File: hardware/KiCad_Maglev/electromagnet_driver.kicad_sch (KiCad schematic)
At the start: 29 parts, among them J5 621008245821, J6 621006245821

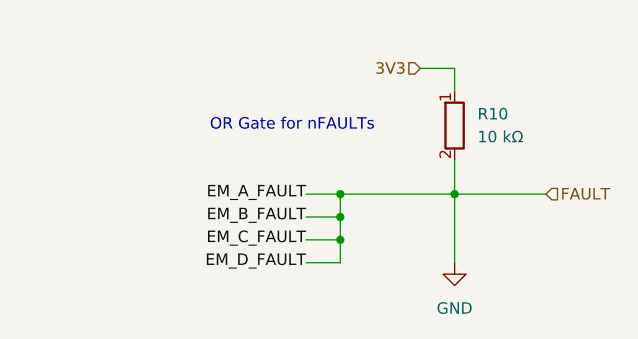
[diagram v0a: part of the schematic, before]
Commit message: some changes to pcb schmatic, added datasheets for used components and linked wurth repo
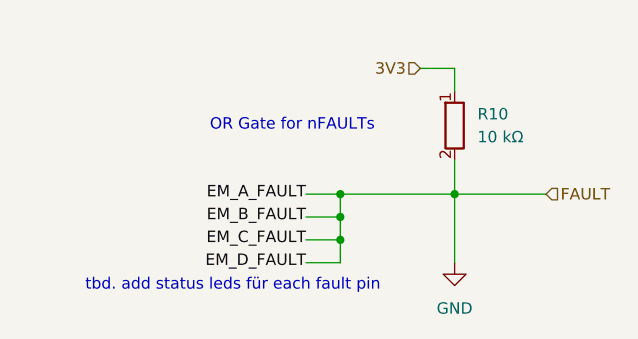
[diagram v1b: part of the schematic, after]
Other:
- note added: "tbd. add status leds für each fault pin"
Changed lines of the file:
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@@
+		)
+	)
+	(text "tbd. add status leds für each fault pin"
+		(exclude_from_sim no)
+		(at 35.052 185.42 0)
+		(effects
+			(font
+				(size 1.27 1.27)
+			)
 		)
 	)

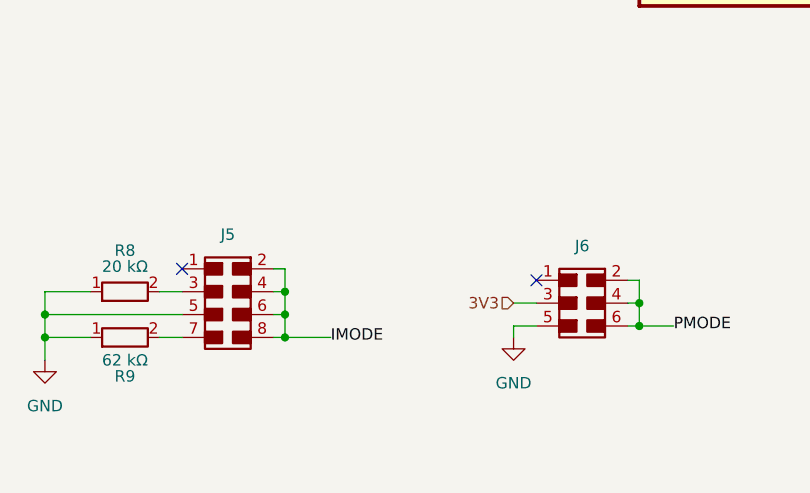
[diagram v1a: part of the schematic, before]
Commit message: Update KiCad schematic sheets
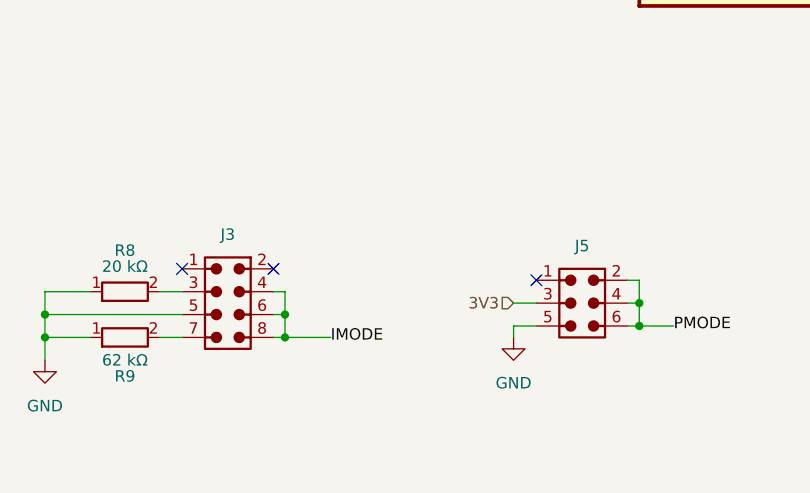
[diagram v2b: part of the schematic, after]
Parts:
- removed J5: 621008245821, Connector_SMD_Wurth:J_Wurth_WR-PHD_621008245821, symbol Connector_Wurth_WR-PHD:621008245821
- removed J6: 621006245821, Connector_SMD_Wurth:J_Wurth_WR-PHD_621006245821, symbol Connector_Wurth_WR-PHD:621006245821
- added J3: 61300821121, Connector_THT_Wurth:J_Wurth_WR-PHD_61300821121, symbol Connector_Wurth_WR-PHD:61300821121
- added J5: 61300621121, Connector_THT_Wurth:J_Wurth_WR-PHD_61300621121, symbol Connector_Wurth_WR-PHD:61300621121
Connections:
- net 3V3: now also J5.3
- net GND: now also J3.5, J5.5
- net IMODE: now also J3.4, J3.6, J3.8
- net PMODE: now also J5.2, J5.4, J5.6
- net at R8.2: now also J3.3
- net at R9.2: now also J3.7
- no-connect marks 2 -> 3

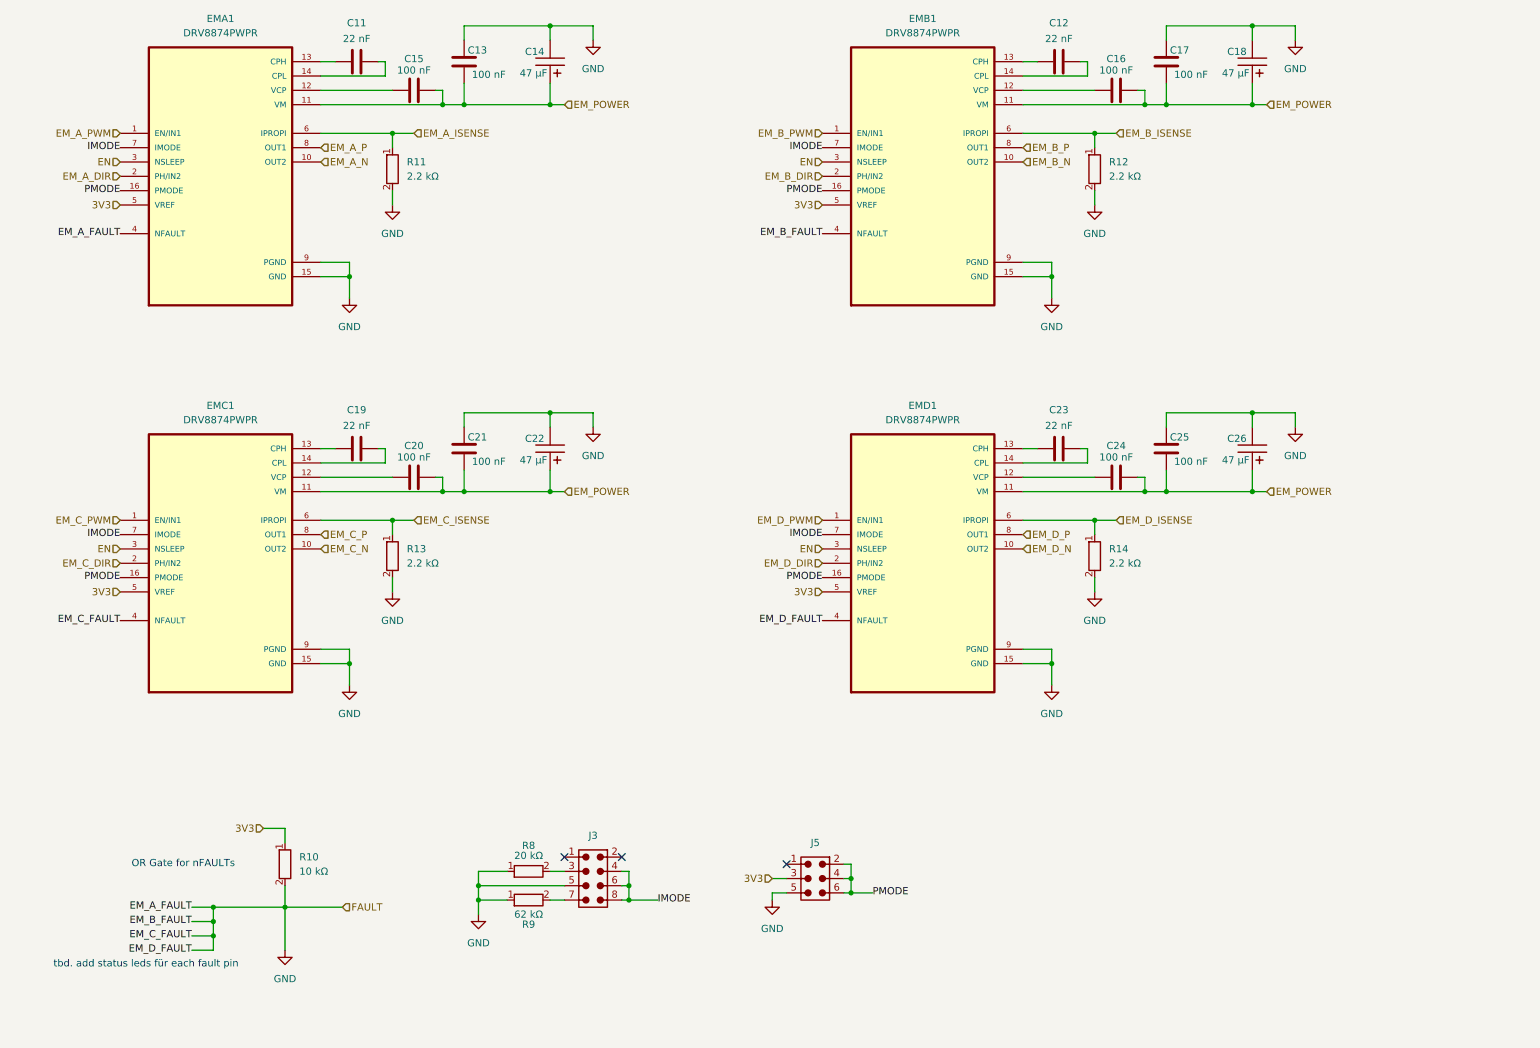
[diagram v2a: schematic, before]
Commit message: Added Footprints/Models for coil and ringmagnet, changed most components to 1206 series
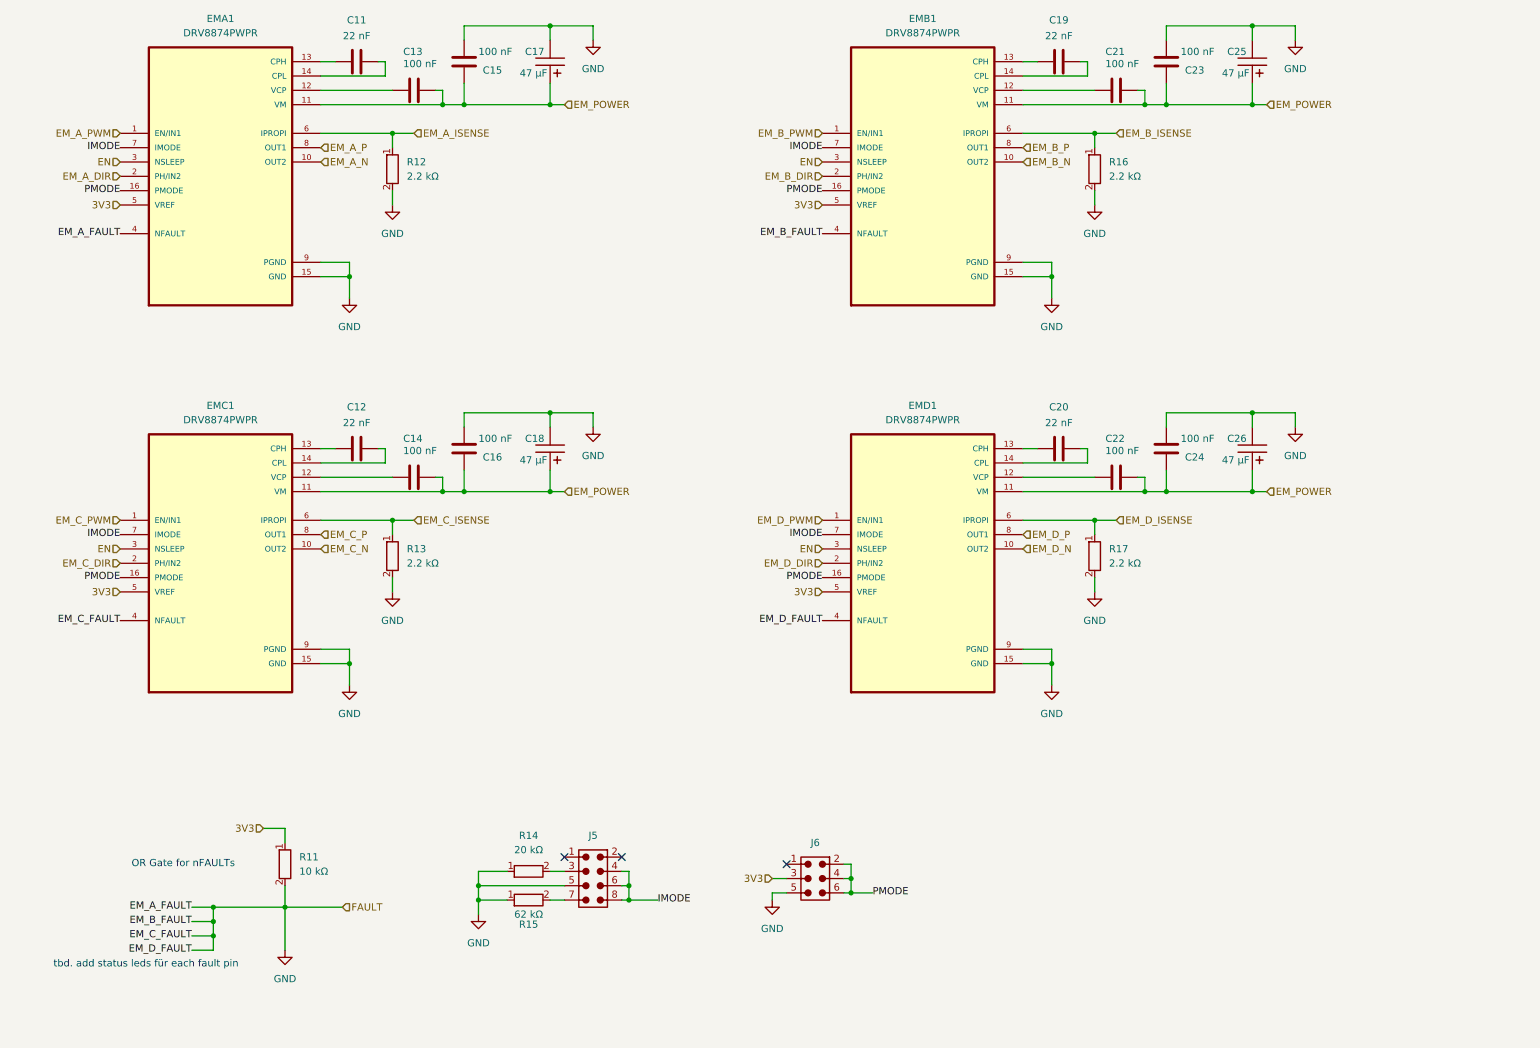
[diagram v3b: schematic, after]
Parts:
- removed C11, C12, C19, C23: 0805_H1.25_R_885342207011, Capacitor_SMD_Wurth:C_Wurth_WCAP-CSMH-0805_H1.25_R, symbol Capacitor_Wurth_WCAP-CSMH:0805_H1.25_R_885342207011
- removed C13, C15, C16, C17, C20, C21, C24, C25: 0603_R_885012206095, Capacitor_SMD_Wurth:C_Wurth_WCAP-CSGP-0603_R, symbol Capacitor_Wurth_WCAP-CSGP:0603_R_885012206095
- removed R10: 0603_R_560112116005, Resistor_SMD_Wurth:R_Wurth_WRIS-RSKS-0603_R, symbol Resistor_Wurth_WRIS-RSKS:0603_R_560112116005
- removed R11, R12, R13, R14: 0603_R_560112116098, Resistor_SMD_Wurth:R_Wurth_WRIS-RSKS-0603_R, symbol Resistor_Wurth_WRIS-RSKS:0603_R_560112116098
- removed R8: 0603_R_560112116015, Resistor_SMD_Wurth:R_Wurth_WRIS-RSKS-0603_R, symbol Resistor_Wurth_WRIS-RSKS:0603_R_560112116015
- added C11, C12, C19, C20: 1206_H0.8_885012208083, Capacitor_SMD_Wurth:C_Wurth_WCAP-CSGP-1206_H0.8, symbol Capacitor_Wurth_WCAP-CSGP:1206_H0.8_885012208083
- added C13, C14, C15, C16, C21, C22, C23, C24: 1206_H1.25_885012208118, Capacitor_SMD_Wurth:C_Wurth_WCAP-CSGP-1206_H1.25, symbol Capacitor_Wurth_WCAP-CSGP:1206_H1.25_885012208118
- added R11: 1206_R_560112132018, Resistor_SMD_Wurth:R_Wurth_WRIS-RSKS-1206_R, symbol Resistor_Wurth_WRIS-RSKS:1206_R_560112132018
- added R12, R13, R16, R17: 1206_R_560112132019, Resistor_SMD_Wurth:R_Wurth_WRIS-RSKS-1206_R, symbol Resistor_Wurth_WRIS-RSKS:1206_R_560112132019
- added R14: 1206_R_560112132041, Resistor_SMD_Wurth:R_Wurth_WRIS-RSKS-1206_R, symbol Resistor_Wurth_WRIS-RSKS:1206_R_560112132041
- renumbered C14 to C17, C22 to C18, C18 to C25, J3 to J5, J5 to J6, R9 to R15
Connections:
- net 3V3: now also R11.1
- net EM_A_ISENSE: now also R12.1
- net EM_B_ISENSE: now also R16.1
- net EM_C_ISENSE: now also R13.1
- net EM_D_ISENSE: now also R17.1
- net EM_POWER: now also C13.2, C14.2, C15.1, C16.1, C21.2, C22.2, C23.1, C24.1
- net GND: now also C15.2, C16.2, C23.2, C24.2, R11.2, R12.2, R13.2, R14.1, R16.2, R17.2
- net at EMA1.12 (VCP): now also C13.1
- net at EMD1.13 (CPH): now also C20.1
- net at EMD1.14 (CPL): now also C20.2
- net at EMA1.13 (CPH): now also C11.1
- net at EMA1.14 (CPL): now also C11.2
- net at EMC1.12 (VCP): now also C14.1
- net at J5.3: now also R14.2
- net at EMB1.12 (VCP): now also C21.1
- net at EMB1.13 (CPH): now also C19.1
- net at EMB1.14 (CPL): now also C19.2
- net at EMC1.13 (CPH): now also C12.1
- net at EMC1.14 (CPL): now also C12.2
- net at EMD1.12 (VCP): now also C22.1

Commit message: changed mounting and spacing system and  some detail changes
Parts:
- EMA1, EMB1, EMC1, EMD1: footprint SOP65P640X120-17N -> SOP65P640X120-17N:SOP65P640X120-17N
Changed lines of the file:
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@@
 			)
 		)
-		(property "Footprint" "SOP65P640X120-17N"
+		(property "Footprint" "SOP65P640X120-17N:SOP65P640X120-17N"
 			(at 48.26 45.72 0)
 			(hide yes)
@@
 			)
 		)
-		(property "Footprint" "SOP65P640X120-17N"
+		(property "Footprint" "SOP65P640X120-17N:SOP65P640X120-17N"
 			(at 172.72 45.72 0)
 			(hide yes)
@@
 			)
 		)
-		(property "Footprint" "SOP65P640X120-17N"
+		(property "Footprint" "SOP65P640X120-17N:SOP65P640X120-17N"
 			(at 172.72 114.3 0)
 			(hide yes)
@@
 			)
 		)
-		(property "Footprint" "SOP65P640X120-17N"
+		(property "Footprint" "SOP65P640X120-17N:SOP65P640X120-17N"
 			(at 48.26 114.3 0)
 			(hide yes)

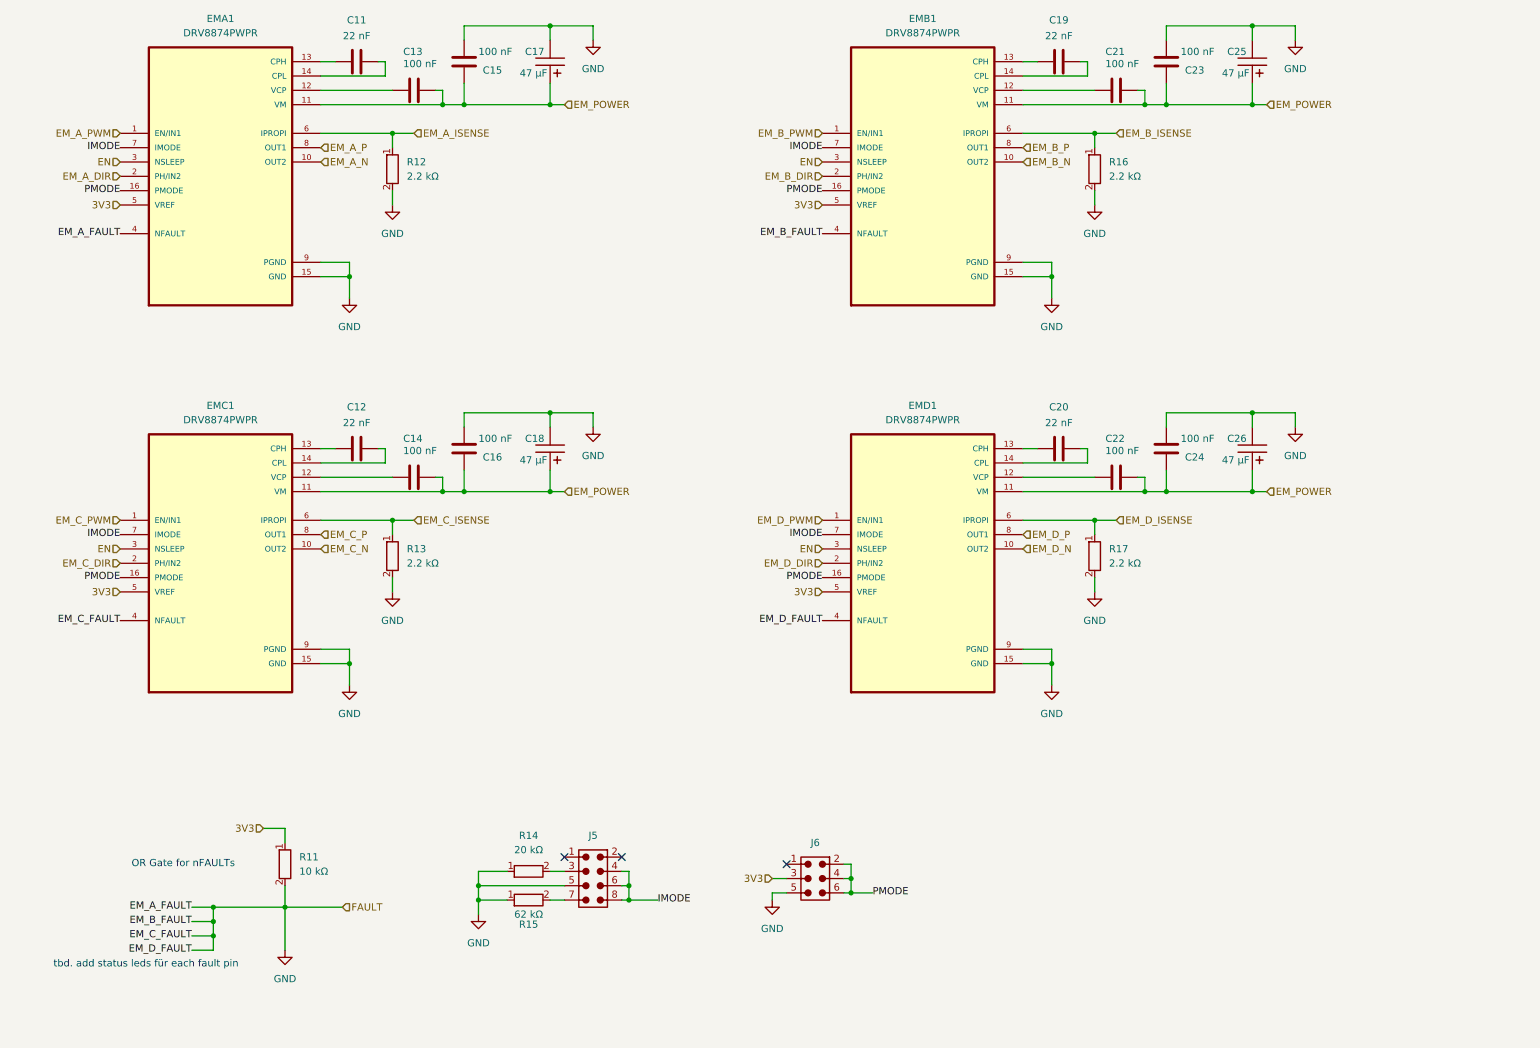
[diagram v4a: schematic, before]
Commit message: Mistake in H-Bridge schematic - required rerouting
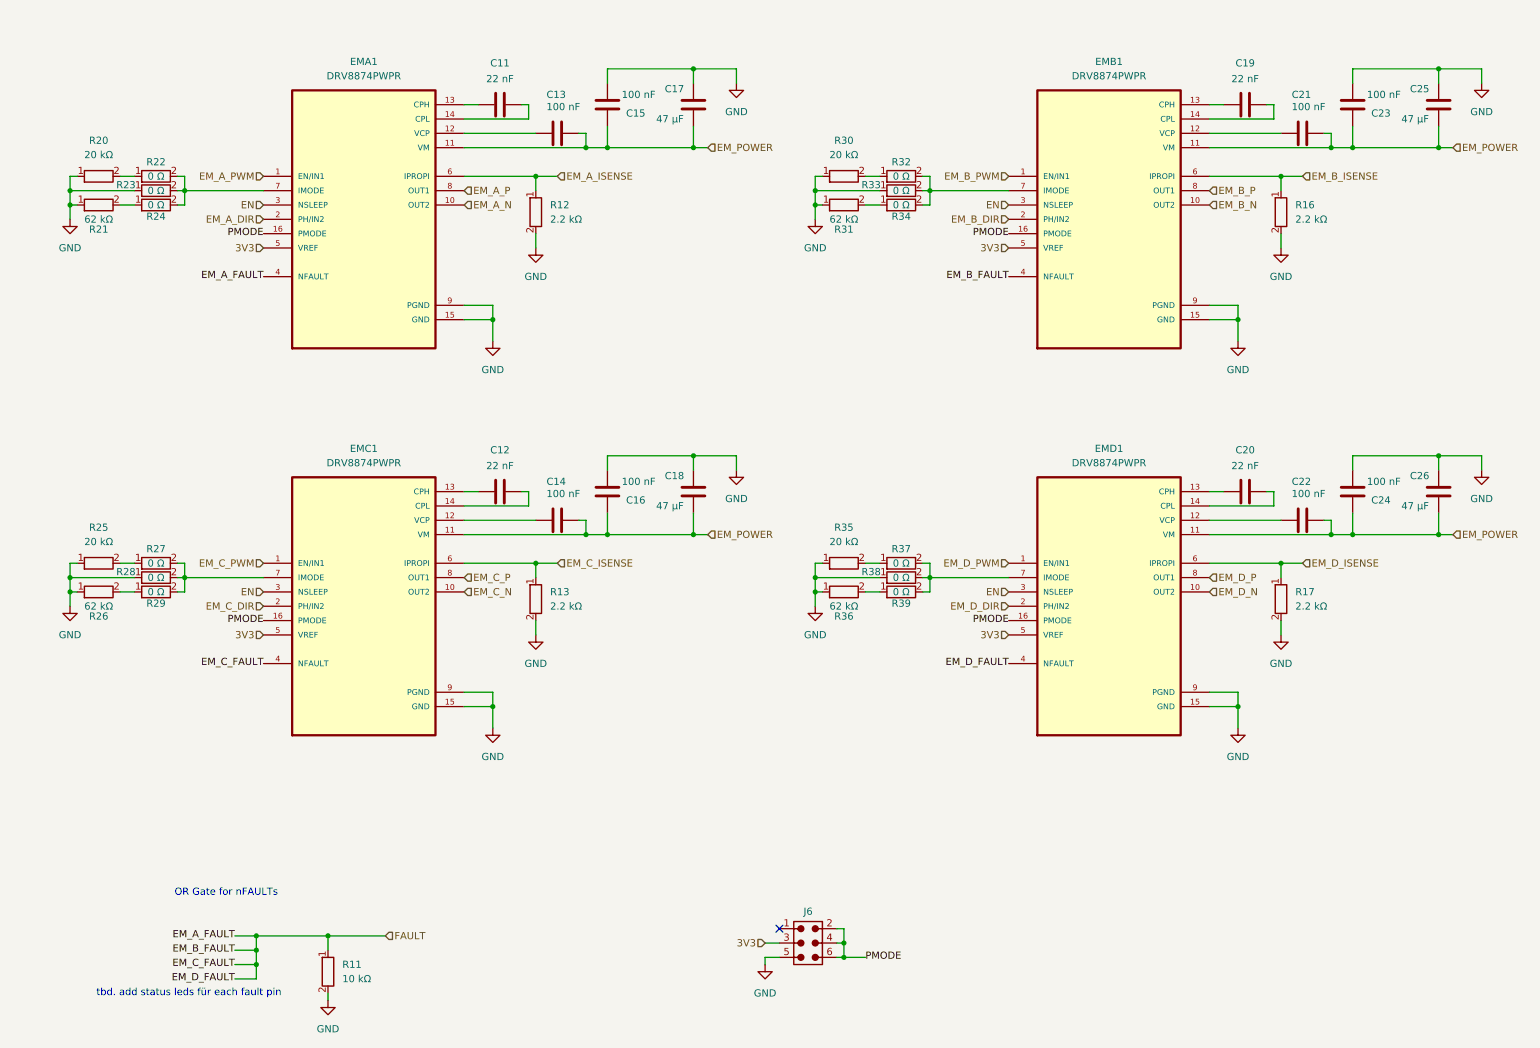
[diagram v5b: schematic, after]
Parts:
- removed C17, C18, C25, C26: D8L11.5_870585774003, Capacitor_THT_Wurth:CP_Wurth_WCAP-HTAH-D8L11.5, symbol Capacitor_Wurth_WCAP-HTAH:D8L11.5_870585774003
- removed J5: 61300821121, Connector_THT_Wurth:J_Wurth_WR-PHD_61300821121, symbol Connector_Wurth_WR-PHD:61300821121
- removed R14: 1206_R_560112132041, Resistor_SMD_Wurth:R_Wurth_WRIS-RSKS-1206_R, symbol Resistor_Wurth_WRIS-RSKS:1206_R_560112132041
- removed R15: 0603_R_560112116048, Resistor_SMD_Wurth:R_Wurth_WRIS-RSKS-0603_R, symbol Resistor_Wurth_WRIS-RSKS:0603_R_560112116048
- added C17, C18, C25, C26: 1210_H2.5_885012109011, Capacitor_SMD_Wurth:C_Wurth_WCAP-CSGP-1210_H2.5, symbol Capacitor_Wurth_WCAP-CSGP:1210_H2.5_885012109011
- added R20, R25, R30, R35: 1206_R_560112132041, Resistor_SMD_Wurth:R_Wurth_WRIS-RSKS-1206_R, symbol Resistor_Wurth_WRIS-RSKS:1206_R_560112132041
- added R21, R26, R31, R36: 0603_R_560112116048, Resistor_SMD_Wurth:R_Wurth_WRIS-RSKS-0603_R, symbol Resistor_Wurth_WRIS-RSKS:0603_R_560112116048
- added R22, R23, R24, R27, R28, R29, R32, R33, R34, R37, R38, R39: 0805_R_560112120002, Resistor_SMD_Wurth:R_Wurth_WRIS-RSKS-0805_R, symbol Resistor_Wurth_WRIS-RSKS:0805_R_560112120002
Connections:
- net 3V3: no longer R11.1
- net EM_POWER: now also C17.2, C18.2, C25.2, C26.2
- net GND: now also C17.1, C18.1, C25.1, C26.1, R20.1, R21.1, R23.1, R25.1, R26.1, R28.1, R30.1, R31.1, R33.1, R35.1, R36.1, R38.1; no longer EMA1.4 (NFAULT), EMB1.4 (NFAULT), EMC1.4 (NFAULT), EMD1.4 (NFAULT)
- removed net IMODE: EMA1.7 (IMODE), EMB1.7 (IMODE), EMC1.7 (IMODE), EMD1.7 (IMODE)
- new net: R25.2, R27.1
- new net: R36.2, R39.1
- new net: R20.2, R22.1
- new net: R21.2, R24.1
- new net: EMA1.7 (IMODE), R22.2, R23.2, R24.2
- new net: R26.2, R29.1
- new net: R35.2, R37.1
- new net: EMD1.7 (IMODE), R37.2, R38.2, R39.2
- new net: R31.2, R34.1
- new net: R30.2, R32.1
- new net: EMB1.7 (IMODE), R32.2, R33.2, R34.2
- new net: EMC1.7 (IMODE), R27.2, R28.2, R29.2
- new net FAULT: EMA1.4 (NFAULT), EMB1.4 (NFAULT), EMC1.4 (NFAULT), EMD1.4 (NFAULT), R11.1
- no-connect marks 3 -> 1
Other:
- moved on the sheet: C11, C12, C13, C14, C15, C16, C19, C20, C21, C22, C23, C24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
